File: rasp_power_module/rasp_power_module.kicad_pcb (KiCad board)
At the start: 2 copper layers, 45 x 57.1 mm, 22 parts, among them J1 Conn_01x02, J2 Conn_01x05, J3 Conn_01x02, J5 Conn_01x02, J7 Conn_01x02, J8 Conn_01x02, J9 Conn_01x02, K1 G5V-1, K2 FINDER-36.11, Q1 BC847

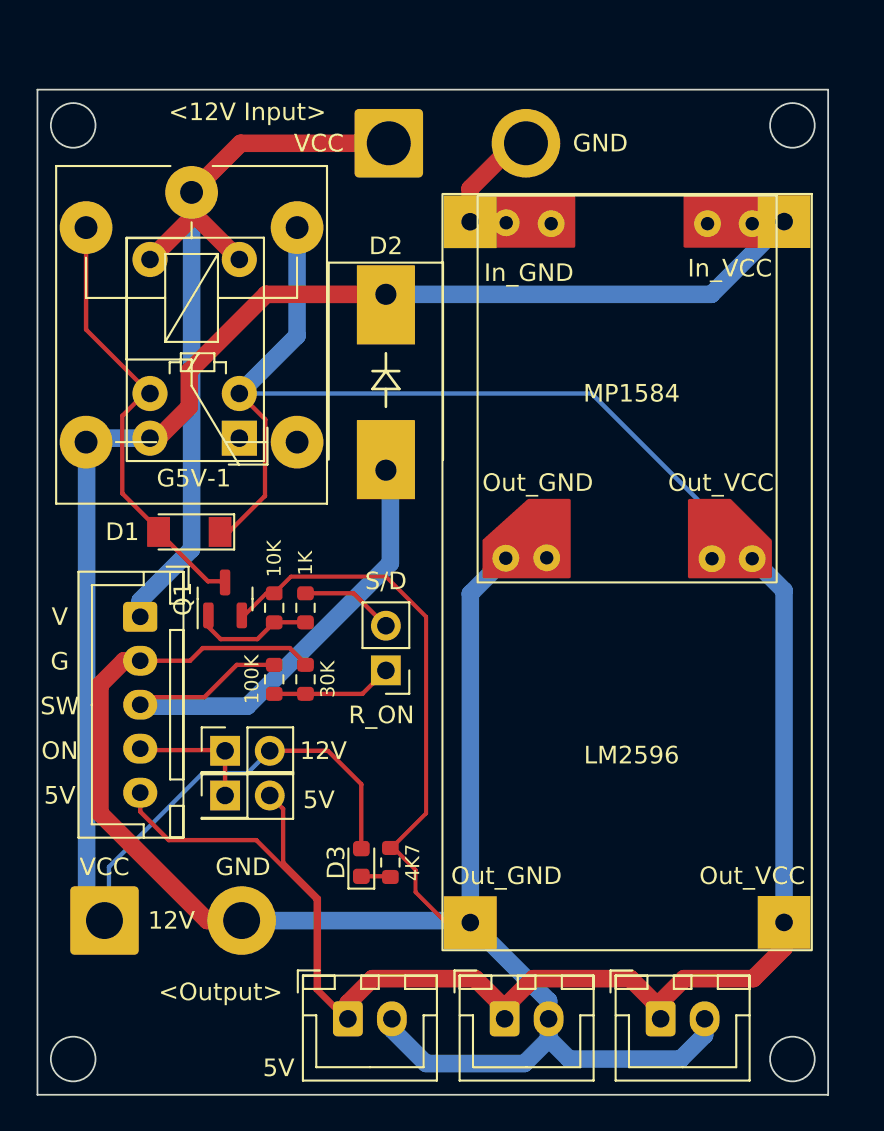
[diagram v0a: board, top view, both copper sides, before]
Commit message: rasp_power_module smt 관련 작업 추가 및 monitor_control_board 개선
Signed-off-by: Ju, Gyeong-min <jcmh74@gmail.com>
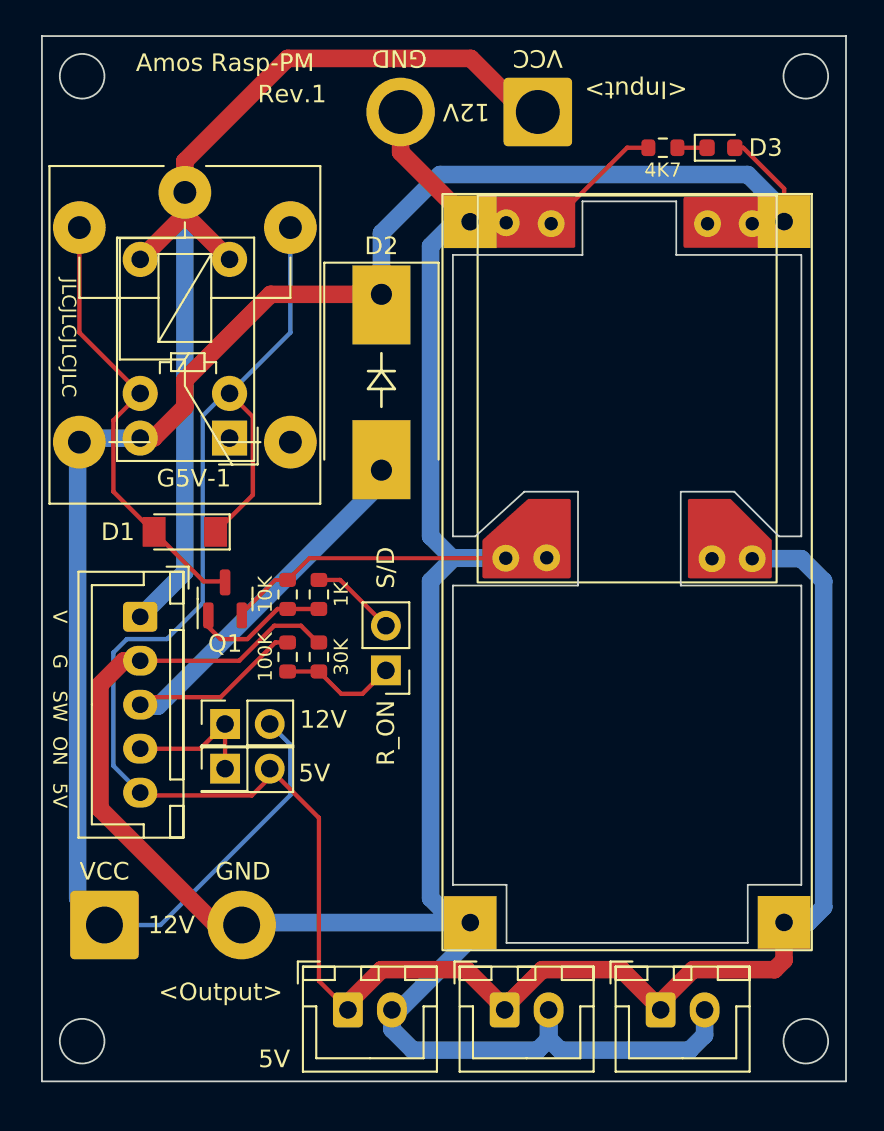
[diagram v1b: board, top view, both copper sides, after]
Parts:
- D1: value ZMM5V1 -> ZMM5V6-M
- Q1: value BC847 -> S8050 J3Y
- moved D3 45.5 mm to (160.3, 63.5), turned to 0 degrees
- moved R5 43.5 mm to (157.0, 63.5), turned to 0 degrees
- moved J1 8.66 mm to (149.9, 61.5), turned to 180 degrees
- moved JP1 1.52 mm to (132.1, 96.3)
- moved JP2 1.52 mm to (132.1, 98.8)
- moved R3 1.48 mm to (135.6, 92.5)
- moved R4 1.48 mm to (137.4, 92.5)
- moved R1 1.08 mm to (137.4, 88.9)
- moved R2 1.08 mm to (135.6, 88.9)
- moved K1 0.56 mm to (132.3, 80.0)
- moved J7 0.51 mm to (139.1, 112.5)
- moved J8 0.51 mm to (148.0, 112.5)
- moved J9 0.51 mm to (156.8, 112.5)
- moved K2 0.38 mm to (129.8, 66.0)
- moved J5 0.25 mm to (125.2, 107.7)
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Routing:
- net InGND: track 143.5 -> 165.7 mm
- net 5V_ON: track 145.8 -> 132.2 mm
- net Relay_In: track 47.4 -> 59.2 mm
- net 12V_ON: track 102.8 -> 107.1 mm
- net /SWITCH: track 31.6 -> 29.6 mm
- net Net-(Q1-Pad1): track 6.86 -> 7.94 mm
- net /ON_LED: track 7.42 -> 7.95 mm
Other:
- board size 45 x 57.1 mm -> 45.7 x 59.4 mm
- board text added: "<-MP1584 Out"
- board text added: "<Input>"
- board text added: "Amos Rasp-PM"
- board text added: "JLCJLCJLCJLC"
- board text added: "Rev.1"
- board text removed: "<12V Input>"

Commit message: rasp-power-module 마커 변경
Signed-off-by: Ju, Gyeong-min <jcmh74@gmail.com>
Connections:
- J3 pad 1: /POWER_SIG -> /SHUTDOWN
- J3 pad 2: /SHUTDOWN -> /POWER_SIG
- R1 pad 1: /SHUTDOWN -> /POWER_SIG
- R3 pad 2: /POWER_SIG -> /SHUTDOWN
- R4 pad 2: /POWER_SIG -> /SHUTDOWN
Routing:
- net /SHUTDOWN: track 4.89 -> 6.67 mm
- net /POWER_SIG: track 6.67 -> 4.89 mm
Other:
- board text added: "ON(I)"
- board text added: "S/D(O)"
- board text removed: "R_ON"
- board text removed: "S/D"
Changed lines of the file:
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@@
     (fp_line (start 0.8 0.4125) (end -0.8 0.4125) (layer "F.Fab") (width 0.1))
     (pad "1" smd roundrect (at -0.825 0 270) (size 0.8 0.95) (layers "F.Cu" "F.Paste" "F.Mask") (roundrect_rratio 0.25)
-      (net 10 "/SHUTDOWN") (pintype "passive"))
+      (net 9 "/POWER_SIG") (pintype "passive"))
     (pad "2" smd roundrect (at 0.825 0 270) (size 0.8 0.95) (layers "F.Cu" "F.Paste" "F.Mask") (roundrect_rratio 0.25)
       (net 13 "Net-(Q1-Pad1)") (pintype "passive"))
@@
       (net 5 "InGND") (pintype "passive"))
     (pad "2" smd roundrect (at 0.825 0 270) (size 0.8 0.95) (layers "F.Cu" "F.Paste" "F.Mask") (roundrect_rratio 0.25)
-      (net 9 "/POWER_SIG") (pintype "passive"))
+      (net 10 "/SHUTDOWN") (pintype "passive"))
     (model "${KICAD6_3DMODEL_DIR}/Resistor_SMD.3dshapes/R_0603_1608Metric.wrl"
       (offset (xyz 0 0 0))
@@
     (fp_line (start 1.27 3.81) (end -1.27 3.81) (layer "F.Fab") (width 0.1))
     (pad "1" thru_hole rect (at 0 0 180) (size 1.7 1.7) (drill 1) (layers *.Cu *.Mask)
-      (net 9 "/POWER_SIG") (pinfunction "Pin_1") (pintype "passive"))
+      (net 10 "/SHUTDOWN") (pinfunction "Pin_1") (pintype "passive"))
     (pad "2" thru_hole oval (at 0 2.54 180) (size 1.7 1.7) (drill 1) (layers *.Cu *.Mask)
-      (net 10 "/SHUTDOWN") (pinfunction "Pin_2") (pintype "passive"))
+      (net 9 "/POWER_SIG") (pinfunction "Pin_2") (pintype "passive"))
     (model "${KICAD6_3DMODEL_DIR}/Connector_PinHeader_2.54mm.3dshapes/PinHeader_1x02_P2.54mm_Vertical.wrl"
       (offset (xyz 0 0 0))
@@
       (net 6 "/SWITCH") (pintype "passive"))
     (pad "2" smd roundrect (at 0.825 0 270) (size 0.8 0.95) (layers "F.Cu" "F.Paste" "F.Mask") (roundrect_rratio 0.25)
-      (net 9 "/POWER_SIG") (pintype "passive"))
+      (net 10 "/SHUTDOWN") (pintype "passive"))
     (model "${KICAD6_3DMODEL_DIR}/Resistor_SMD.3dshapes/R_0603_1608Metric.wrl"
       (offset (xyz 0 0 0))
@@
       (xy 151.638 83.566)
     ) (layer "F.Cu") (width 0.2) (fill solid))
+  (gr_line (start 142.554 90.648) (end 143.256 90.17) (layer "F.SilkS") (width 0.15))
   (gr_line (start 140.97 77.216) (end 140.97 78.232) (layer "F.SilkS") (width 0.15))
   (gr_line (start 140.208 77.216) (end 141.732 77.216) (layer "F.SilkS") (width 0.15))
+  (gr_line (start 143.256 90.17) (end 143.256 88.9) (layer "F.SilkS") (width 0.15))
   (gr_line (start 140.97 76.2) (end 140.208 77.216) (layer "F.SilkS") (width 0.15))
+  (gr_line (start 143.256 93.726) (end 143.256 94.996) (layer "F.SilkS") (width 0.15))
+  (gr_line (start 142.554 93.218) (end 143.256 93.726) (layer "F.SilkS") (width 0.15))
   (gr_line (start 140.97 75.184) (end 140.97 76.2) (layer "F.SilkS") (width 0.15))
   (gr_line (start 141.732 77.216) (end 140.97 76.2) (layer "F.SilkS") (width 0.15))
@@
     (effects (font (size 1 1) (thickness 0.15)))
   )
-  (gr_text "S/D" (at 141.224 87.376 90) (layer "F.SilkS")
+  (gr_text "S/D(O)" (at 143.256 97.79 90) (layer "F.SilkS")
     (effects (font (size 1 1) (thickness 0.15)))
   )
@@
     (effects (font (size 0.8 0.8) (thickness 0.15)))
   )
-  (gr_text "R_ON" (at 141.224 96.774 90) (layer "F.SilkS")
+  (gr_text "ON(I)" (at 143.256 86.614 90) (layer "F.SilkS")
     (effects (font (size 1 1) (thickness 0.15)))
   )
@@
   (segment (start 127.254 97.67) (end 130.676 97.67) (width 0.25) (layer "F.Cu") (net 8))
   (segment (start 130.676 97.67) (end 132.08 96.266) (width 0.25) (layer "F.Cu") (net 8))
-  (segment (start 139.891 94.551) (end 141.224 93.218) (width 0.25) (layer "F.Cu") (net 9))
-  (segment (start 138.684 94.551) (end 139.891 94.551) (width 0.25) (layer "F.Cu") (net 9))
-  (segment (start 137.414 93.281) (end 138.684 94.551) (width 0.25) (layer "F.Cu") (net 9))
-  (segment (start 135.636 93.281) (end 137.414 93.281) (width 0.25) (layer "F.Cu") (net 9))
-  (segment (start 141.224 90.678) (end 138.621 88.075) (width 0.25) (layer "F.Cu") (net 10))
-  (segment (start 138.621 88.075) (end 137.414 88.075) (width 0.25) (layer "F.Cu") (net 10))
+  (segment (start 141.224 90.678) (end 138.621 88.075) (width 0.25) (layer "F.Cu") (net 9))
+  (segment (start 138.621 88.075) (end 137.414 88.075) (width 0.25) (layer "F.Cu") (net 9))
+  (segment (start 139.891 94.551) (end 141.224 93.218) (width 0.25) (layer "F.Cu") (net 10))
+  (segment (start 138.684 94.551) (end 139.891 94.551) (width 0.25) (layer "F.Cu") (net 10))
+  (segment (start 137.414 93.281) (end 138.684 94.551) (width 0.25) (layer "F.Cu") (net 10))
+  (segment (start 135.636 93.281) (end 137.414 93.281) (width 0.25) (layer "F.Cu") (net 10))
   (segment (start 135.636 58.42) (end 129.794 64.262) (width 1) (layer "F.Cu") (net 12))
   (segment (start 149.098 61.468) (end 146.05 58.42) (width 1) (layer "F.Cu") (net 12))

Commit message: rev.2 버전업
Signed-off-by: Ju, Gyeong-min <jcmh74@gmail.com>
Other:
- board text added: "Rev.2"
- board text removed: "Rev.1"
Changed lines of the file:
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@@
     (effects (font (size 1 1) (thickness 0.15)))
   )
-  (gr_text "Rev.1" (at 135.89 60.452) (layer "F.SilkS")
+  (gr_text "Rev.2" (at 135.89 60.452) (layer "F.SilkS")
     (effects (font (size 1 1) (thickness 0.15)))
   )

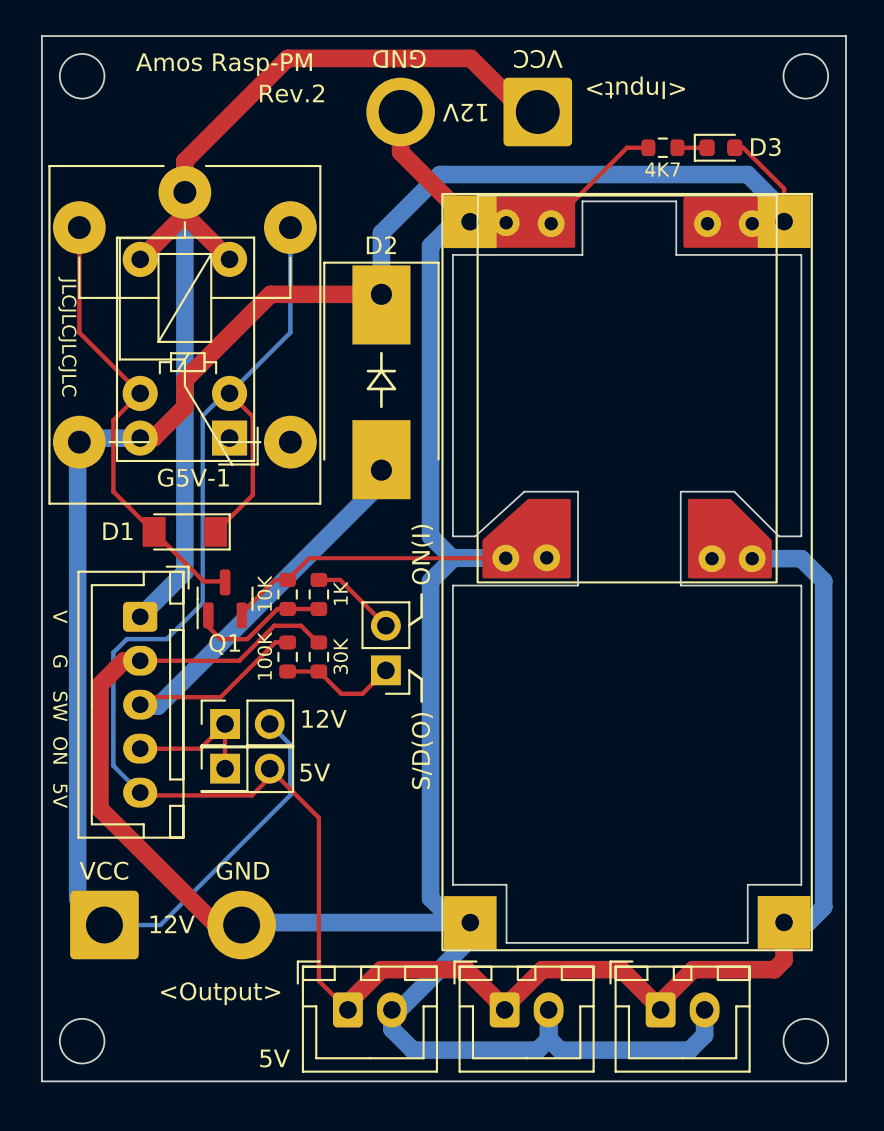
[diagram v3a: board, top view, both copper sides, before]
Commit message: rasp_pm의 MP1584 모듈 실측치 적용
Signed-off-by: Ju, Gyeong-min <jcmh74@gmail.com>
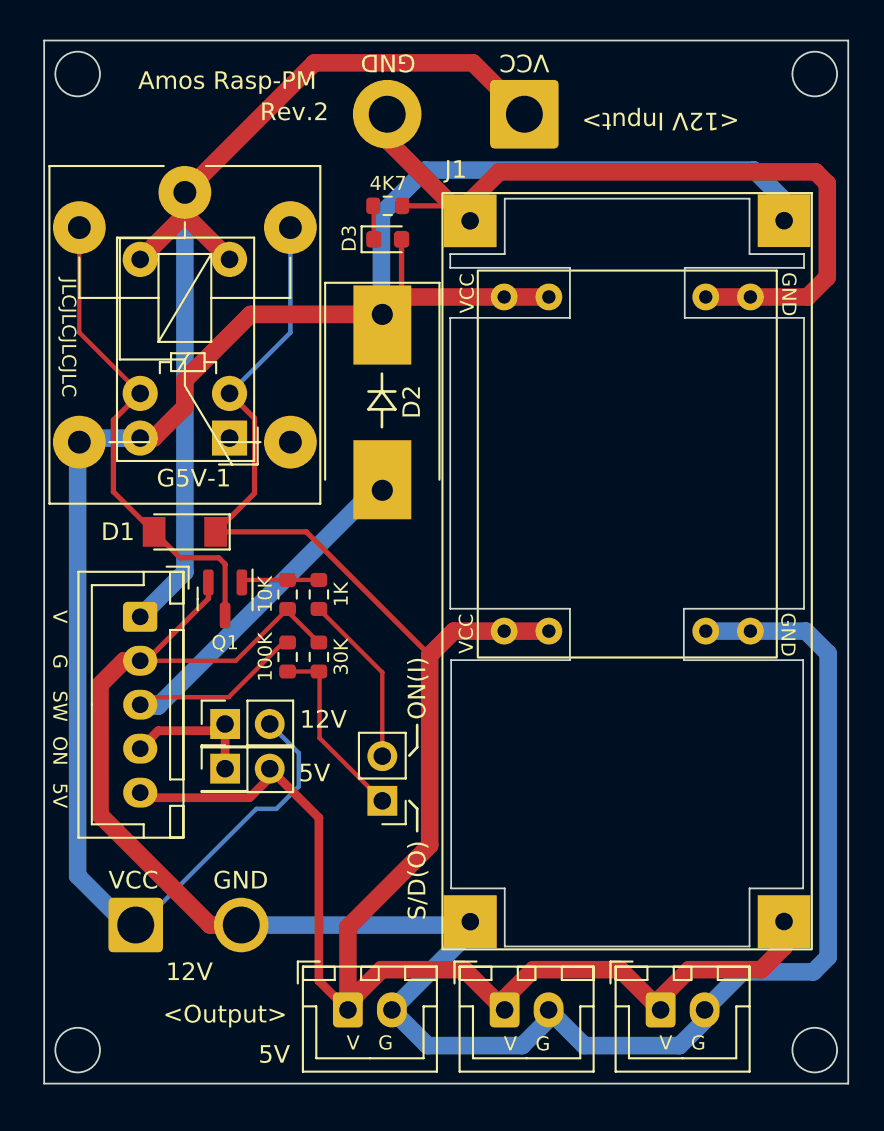
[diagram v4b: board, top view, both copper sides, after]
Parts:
- J1: footprint Connector_Wire:SolderWire-2sqmm_1x02_P7.8mm_D2mm_OD3.9mm -> Connector_Wire:SolderWire-1.5sqmm_1x02_P7.8mm_D1.7mm_OD3.9mm
- J5: footprint Connector_Wire:SolderWire-1.5sqmm_1x02_P7.8mm_D1.7mm_OD3.9mm -> Connector_Wire:SolderWire-1.5sqmm_1x02_P6mm_D1.7mm_OD3mm
- moved D3 19.7 mm to (141.3, 68.7)
- moved R5 16.0 mm to (141.3, 66.8), turned to 180 degrees
- moved DCDC1 10.8 mm to (163.4, 70.5)
- moved J3 7.42 mm to (141.0, 100.6)
- moved J5 1.78 mm to (127.0, 107.7)
- moved D2 1.14 mm to (141.0, 78.0)
- moved J1 0.77 mm to (149.1, 61.6)
- moved DCDC2 0.05 mm to (154.9, 87.6)
- turned Q1 to -90 degrees
- turned R1 to 90 degrees
- turned R2 to 90 degrees
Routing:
- net 5V_ON: track 132.2 -> 120.9 mm
- net 12V_ON: track 107.1 -> 113.3 mm
- net /POWER_SIG: track 4.89 -> 9.86 mm
- net InGND: track 165.7 -> 161.3 mm
- net /SHUTDOWN: track 6.67 -> 10.6 mm
- net Net-(Q1-Pad1): track 7.94 -> 4.44 mm
- net Relay_Coil_2: track 25.3 -> 28.1 mm
- net Relay_In: track 59.2 -> 57.2 mm
- net /SWITCH: track 29.6 -> 28.7 mm
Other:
- board size 45.7 x 59.4 mm -> 45.7 x 59.3 mm
- board text added: "<12V Input>"
- board text added: "G V"
- board text added: "V G"
- board text removed: "<Input>"

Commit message: rasp_pm의 smd 부품을 0603에서 0805로 변경
Signed-off-by: Ju, Gyeong-min <jcmh74@gmail.com>
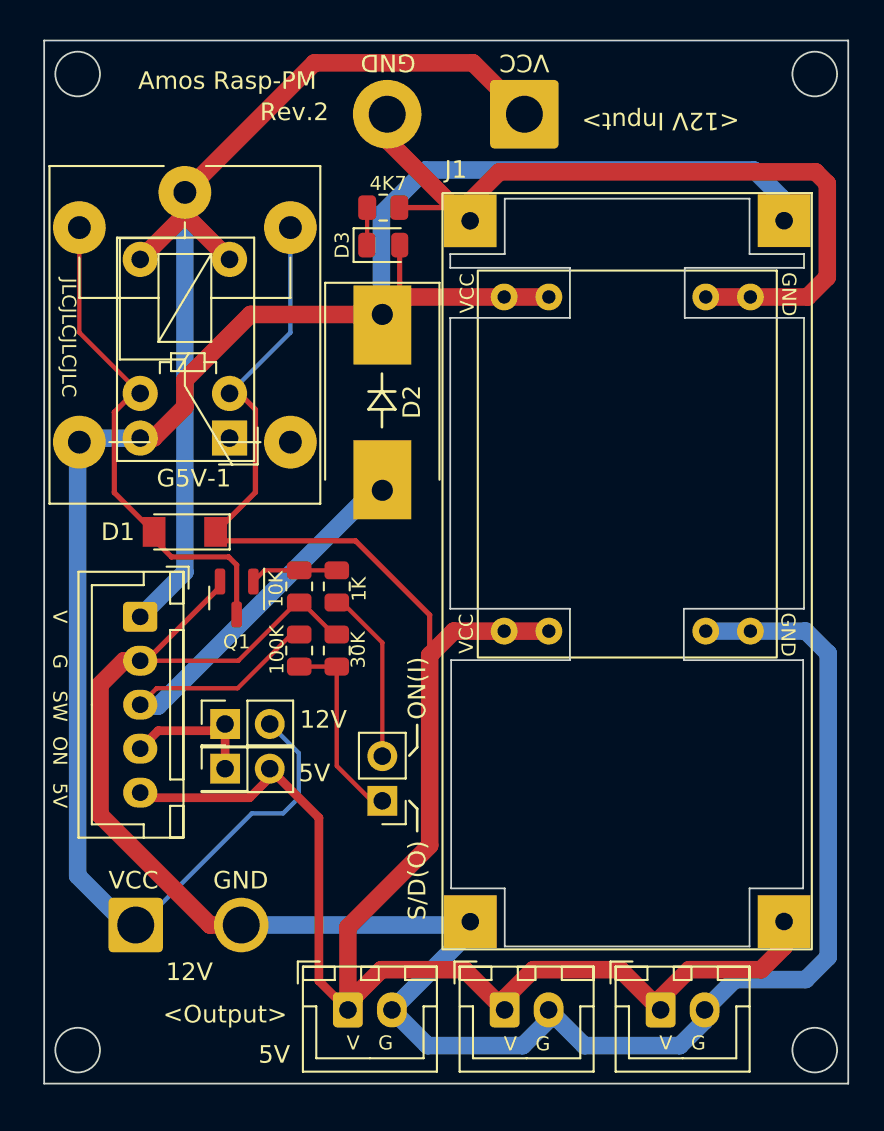
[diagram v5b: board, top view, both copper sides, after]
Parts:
- D3: footprint LED_SMD:LED_0603_1608Metric -> LED_SMD:LED_0805_2012Metric
- R1, R2, R3, R4, R5: footprint Resistor_SMD:R_0603_1608Metric -> Resistor_SMD:R_0805_2012Metric
- moved R1 1.11 mm to (138.4, 88.4)
- moved R4 1.08 mm to (138.4, 92.1)
- moved R2 0.80 mm to (136.3, 88.4)
- moved R3 0.75 mm to (136.3, 92.1)
- moved Q1 0.66 mm to (132.7, 89.1)
- moved D3 0.42 mm to (141.1, 69.0)
- moved R5 0.27 mm to (141.1, 66.9)
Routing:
- net 5V_ON: track 120.9 -> 122.6 mm
- net InGND: track 161.3 -> 162.9 mm
- net /SWITCH: track 28.7 -> 29.8 mm
- net Relay_Coil_2: track 28.1 -> 29.1 mm
- net /SHUTDOWN: track 10.6 -> 11.2 mm
- net Net-(Q1-Pad1): track 4.44 -> 5.00 mm
- net /POWER_SIG: track 9.86 -> 10.4 mm
